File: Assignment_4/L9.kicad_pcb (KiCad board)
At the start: 2 copper layers, 80 x 51 mm, 31 parts, among them J10 USBR, J2 Conn_01x06_Socket, J3 Conn_01x05_Socket, J4 Jack-DC, J5 Conn_01x02_Socket, J6 Conn_01x08_Socket, J7 Conn_01x08_Socket, J8 Conn_01x08_Socket, J9 Conn_01x08_Socket, SW1 SW_Push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

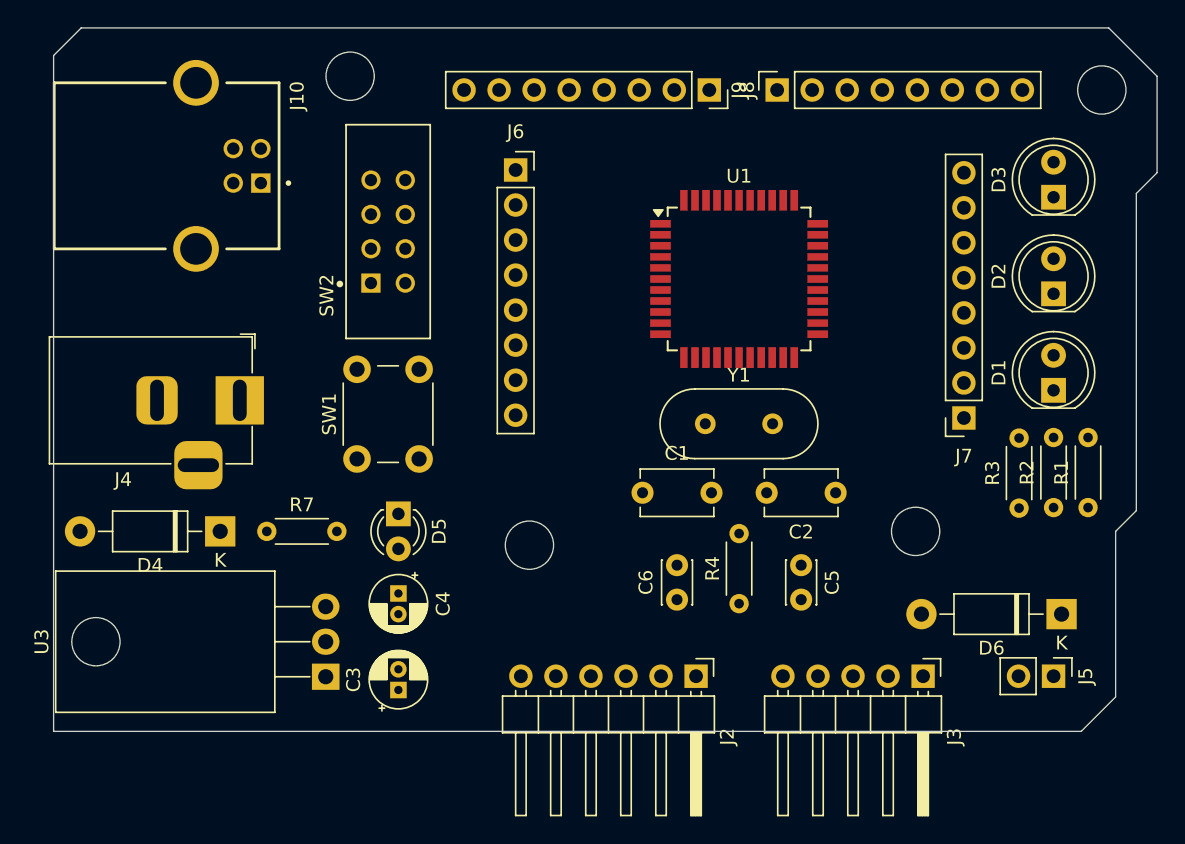
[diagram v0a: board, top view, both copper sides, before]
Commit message: Update layout of all assignments
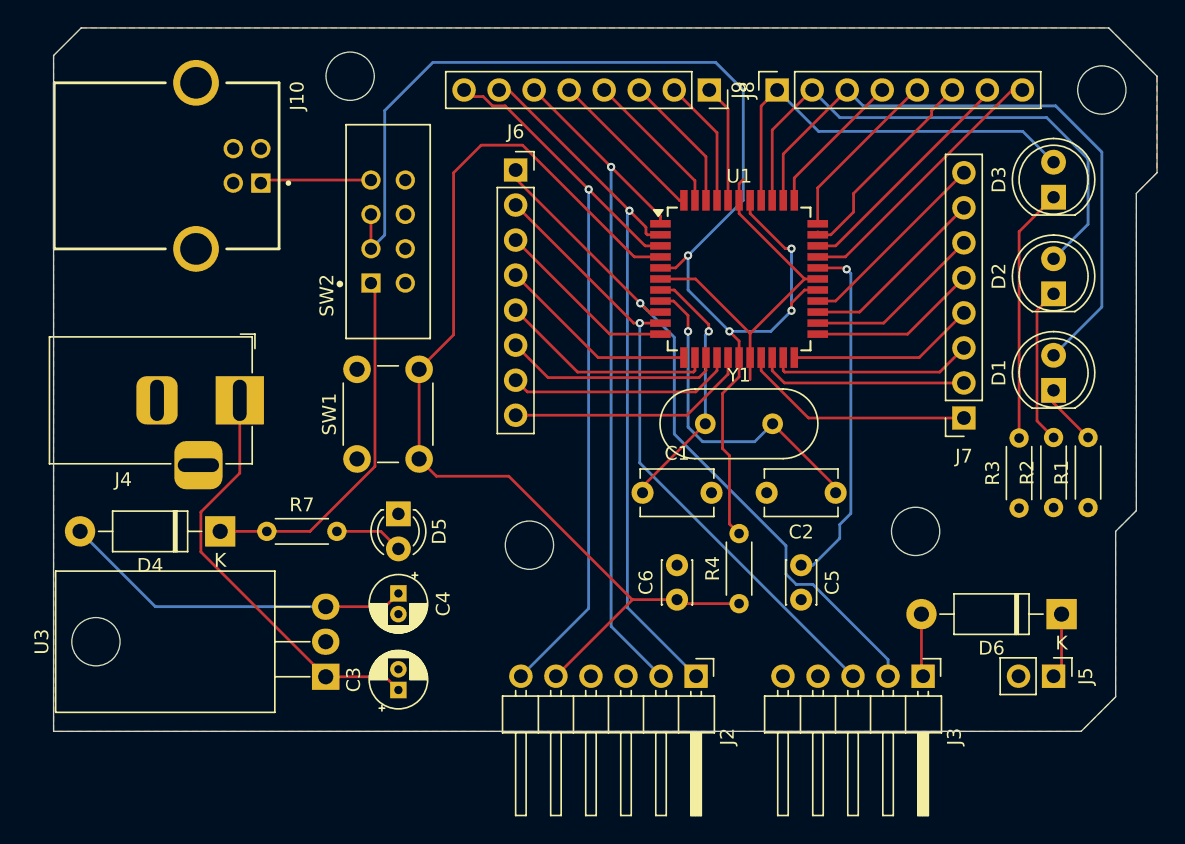
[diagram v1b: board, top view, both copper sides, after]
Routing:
- net MC_VCC: track 0.00 -> 97.4 mm, vias 0 -> 4
- net /RESET: track 0.00 -> 76.4 mm
- net /B7: track 0.00 -> 56.2 mm, vias 0 -> 1
- net /B6: track 0.00 -> 52.2 mm, vias 0 -> 1
- net /B5: track 0.00 -> 51.9 mm, vias 0 -> 1
- net /D0: track 0.00 -> 50.3 mm, vias 0 -> 1
- net /A2: track 0.00 -> 46.4 mm
- net /D1: track 0.00 -> 46.0 mm, vias 0 -> 1
- net /A1: track 0.00 -> 39.5 mm
- net /A0: track 0.00 -> 30.7 mm
- net /12V: track 0.00 -> 30.6 mm
- net GND: track 0.00 -> 27.3 mm
- net /S1_5V: track 0.00 -> 26.6 mm
- net Net-(D4-A): track 0.00 -> 25.7 mm
- net Net-(U1-AREF): track 0.00 -> 25.7 mm, vias 0 -> 1
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- added copper zone on F.Cu, net GND

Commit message: Update layout of all assignments - P2
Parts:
- added G: LOGO, Logo:logo, B.Cu at (95.0, 52.5)
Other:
- board text added: "Name: Ahmed Atef Nasr ID: 1471804251201"
